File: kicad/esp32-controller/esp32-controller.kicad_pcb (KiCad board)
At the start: 2 copper layers, 100.3 x 46.4 mm, 28 parts, among them J1 Barrel_Jack_Switch, J2 RJ45, J3 RJ45, J4 RJ45, J5 RJ45, J6 Conn_01x04_Pin, U1 TPS560430, U2 SN65LVDS049, U3 SN65LVDS049, U4 ESP32-S3-WROOM-1

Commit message: Complete controller PCB v1
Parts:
- added BOOT: SW_Omron_B3FS, Button_Switch_SMD:SW_SPST_Omron_B3FS-100xP, F.Cu at (147.4, 92.0)
- added R7: 10k, Resistor_SMD:R_0805_2012Metric, F.Cu at (153.4, 84.8)
- added RESET: SW_Omron_B3FS, Button_Switch_SMD:SW_SPST_Omron_B3FS-100xP, F.Cu at (136.9, 91.9)
- moved D1 48.9 mm to (100.6, 108.0)
- moved R5 48.9 mm to (104.8, 108.0)
- moved J6 7.60 mm to (154.7, 77.7), turned to 180 degrees
- moved C2 4.51 mm to (127.6, 70.4), turned to 90 degrees
- moved R6 2.65 mm to (130.0, 73.4), turned to 0 degrees
- moved C10 2.54 mm to (130.0, 75.7)
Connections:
- net +5V renamed +12V
- U4 pad 27: unconnected-(U4-IO0-Pad27) -> Net-(U4-IO0)
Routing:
- net Net-(U4-EN): track 0.00 -> 29.9 mm, vias 0 -> 2
- net Net-(U4-IO0): track 0.00 -> 14.5 mm
- net GND: track 26.0 -> 40.4 mm, vias 19 -> 27
- net +3V3: track 0.00 -> 12.4 mm, vias 12 -> 14
- net Net-(J6-Pin_2): track 0.00 -> 4.02 mm
- net Net-(J6-Pin_3): track 0.00 -> 3.89 mm

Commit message: Cleanup
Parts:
- removed BOOT, RESET: SW_Omron_B3FS, Button_Switch_SMD:SW_SPST_Omron_B3FS-100xP
- added BOOT1: SW_Omron_B3FS, Button_Switch_SMD:SW_SPST_Omron_B3FS-100xP, F.Cu at (147.3, 91.9)
- added RESET1: SW_Omron_B3FS, Button_Switch_SMD:SW_SPST_Omron_B3FS-100xP, F.Cu at (136.9, 91.9)
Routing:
- net GND: track 40.4 -> 56.8 mm
- net +12V: track 0.00 -> 9.40 mm
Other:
- board text added: "OUT_0"
- board text added: "OUT_1"
- board text removed: "SN65LVDS049"

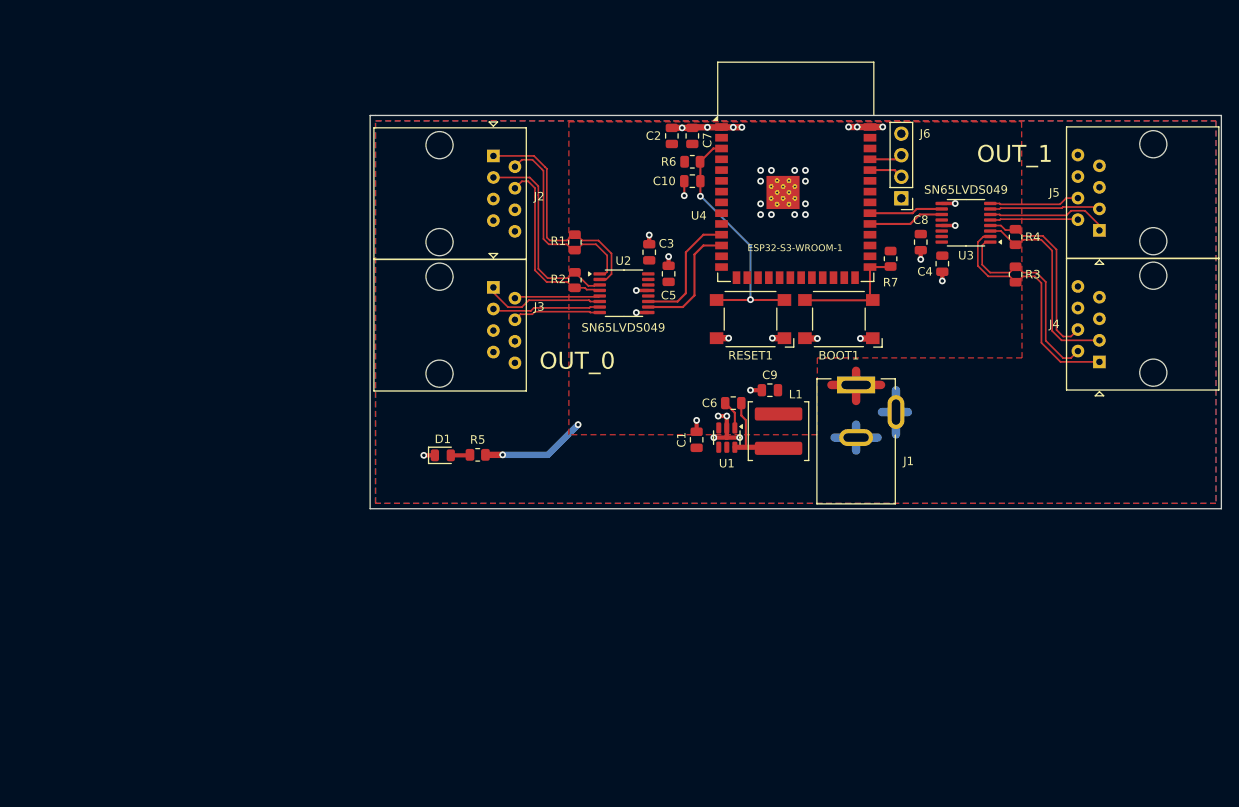
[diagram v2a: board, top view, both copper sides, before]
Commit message: Migrate to 3 chain setup
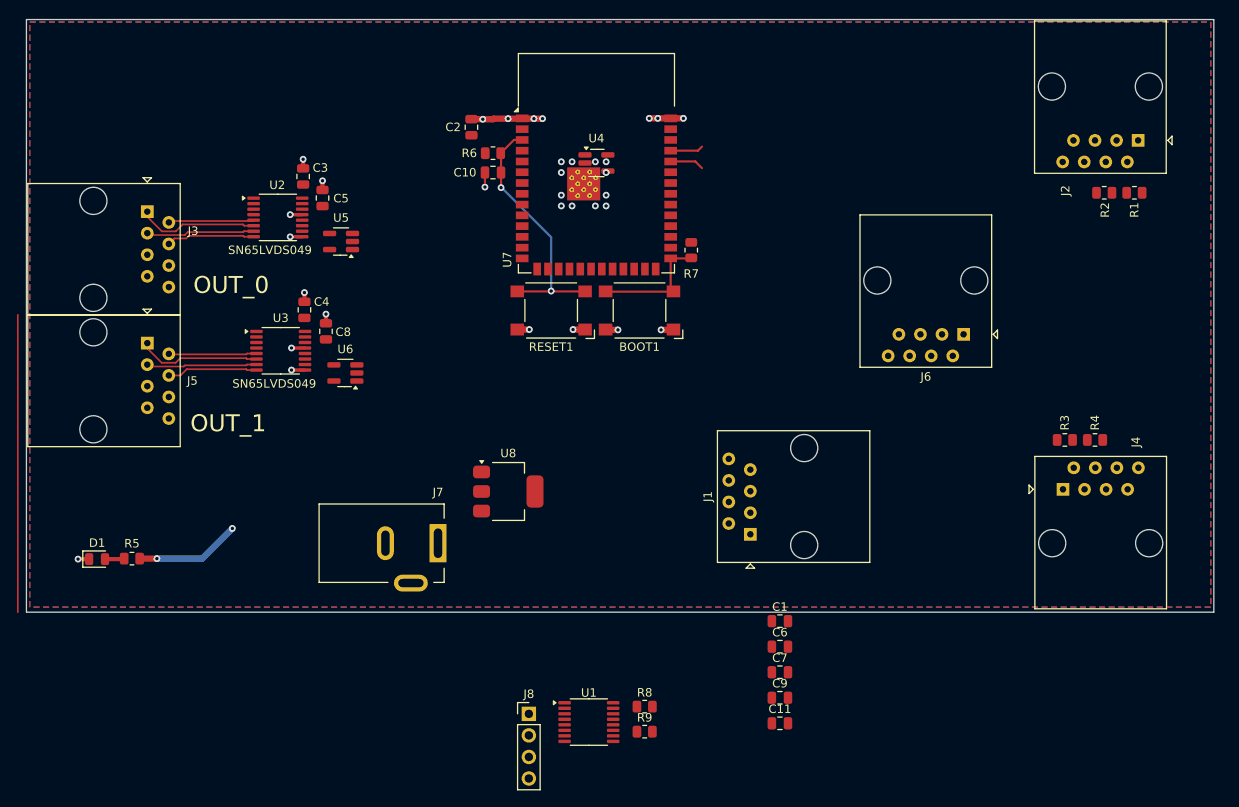
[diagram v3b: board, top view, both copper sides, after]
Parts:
- removed L1: L_Ferrite, Inductor_SMD:L_Bourns_SRP6060FA
- added C11: 100nF, Capacitor_SMD:C_0805_2012Metric, F.Cu at (140.4, 139.6)
- added J7: Barrel_Jack_Switch, Connector_BarrelJack:BarrelJack_Kycon_KLDX-0202-xC_Horizontal, F.Cu at (100.1, 118.4)
- added J8: Conn_01x04_Pin, Connector_PinHeader_2.54mm:PinHeader_1x04_P2.54mm_Vertical, F.Cu at (110.8, 138.5)
- added R8: 10k, Resistor_SMD:R_0805_2012Metric, F.Cu at (124.4, 137.6)
- added R9: 330, Resistor_SMD:R_0805_2012Metric, F.Cu at (124.4, 140.6)
- added U5: 74AHC1G08, Package_TO_SOT_SMD:SOT-23-5_HandSoldering, F.Cu at (88.6, 82.8)
- added U6: 74AHC1G08, Package_TO_SOT_SMD:SOT-23-5_HandSoldering, F.Cu at (89.2, 98.3)
- added U7: ESP32-S3-WROOM-1, RF_Module:ESP32-S3-WROOM-1, F.Cu at (118.7, 73.5)
- added U8: AZ1117-3.3, Package_TO_SOT_SMD:SOT-223-3_TabPin2, F.Cu at (108.4, 112.3)
- C1: value 2.2uF -> 100nF
- C10: value 1uF -> 100nF
- C6: value 100nF -> 4nF
- C7: value 22uF -> 1uF
- C8: value 100nF -> 10uF
- C9: value 100nF -> 22uF
- J1: value Barrel_Jack_Switch -> RJ45; footprint Connector_BarrelJack:BarrelJack_Kycon_KLDX-0202-xC_Horizontal -> Connector_RJ:RJ45_Amphenol_54602-x08_Horizontal
- J6: value Conn_01x04_Pin -> RJ45; footprint Connector_PinHeader_2.54mm:PinHeader_1x04_P2.54mm_Vertical -> Connector_RJ:RJ45_Amphenol_54602-x08_Horizontal
- R5: value 330 -> 100
- R6: value 10k -> 100
- U1: value TPS560430 -> SN65LVDS049; footprint Package_TO_SOT_SMD:SOT-23-6 -> Package_SO:TSSOP-16_4.4x5mm_P0.65mm
- U4: value ESP32-S3-WROOM-1 -> 74AHC1G08; footprint RF_Module:ESP32-S3-WROOM-1 -> Package_TO_SOT_SMD:SOT-23-5_HandSoldering
- moved J5 113.0 mm to (65.8, 94.8), turned to -90 degrees
- moved U3 82.2 mm to (81.5, 95.7), turned to 0 degrees
- moved J2 76.0 mm to (182.6, 70.9), turned to 180 degrees
- moved C4 75.4 mm to (84.3, 90.9), turned to 90 degrees
- moved C8 70.9 mm to (86.9, 93.4), turned to 90 degrees
- moved R1 66.2 mm to (182.2, 77.1), turned to 180 degrees
- moved C7 64.0 mm to (140.4, 133.6), turned to 0 degrees
- moved R2 63.2 mm to (178.6, 77.1), turned to 0 degrees
- moved D1 42.5 mm to (59.9, 120.2)
- moved R5 42.5 mm to (64.0, 120.2)
- moved C5 41.8 mm to (86.5, 77.7)
- moved U2 41.8 mm to (81.2, 80.0)
- moved C3 41.8 mm to (84.2, 75.1)
- moved J3 41.8 mm to (65.8, 79.3)
- moved U1 37.3 mm to (117.9, 139.4), turned to 0 degrees
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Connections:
- BOOT1 pad 2: Net-(U4-IO0) -> Net-(U7-IO0)
- C1 pad 1: +12V -> +3V3
- C10 pad 1: Net-(U4-EN) -> +3V3
- C6 pad 1: Net-(U1-CB) -> +3V3
- C6 pad 2: Net-(U1-SW) -> GND
- C7 pad 1: +3V3 -> Net-(U7-EN)
- C8 pad 1: +3V3 -> +12V
- J1 pad 1: +12V -> /Din_P
- J1 pad 2: GND -> /Din_N
- J1 pad 3: GND -> /Cin_N
- J2 pad 1: /Din_P -> /Dout_P
- J2 pad 2: /Din_N -> /Dout_N
- J2 pad 3: /Cin_N -> /Cout_N
- J2 pad 4: /Cin_P -> /Cout_P
- J3 pad 1: /Dout_P -> /Din_P2
- J3 pad 2: /Dout_N -> /Din_N2
- J3 pad 3: /Cout_N -> /Cin_N2
- J3 pad 4: /Cout_P -> /Cin_P2
- J4 pad 1: /Din_P2 -> /Dout_P2
- J4 pad 2: /Din_N2 -> /Dout_N2
- J4 pad 3: /Cin_N2 -> /Cout_N2
- J4 pad 4: /Cin_P2 -> /Cout_P2
- J5 pad 1: /Dout_P2 -> /Din_P2
- J5 pad 2: /Dout_N2 -> /Din_N2
- J5 pad 3: /Cout_N2 -> /Cin_N2
- J5 pad 4: /Cout_P2 -> /Cin_P2
- J6 pad 1: GND -> /Dout_P2
- J6 pad 2: Net-(J6-Pin_2) -> /Dout_N2
- J6 pad 3: Net-(J6-Pin_3) -> /Cout_N2
- J6 pad 4: +3V3 -> /Cout_P2
- R5 pad 1: +3V3 -> /Din_P2
- R5 pad 2: Net-(D1-A) -> /Din_N2
- R6 pad 1: +3V3 -> /Cin_P2
- R6 pad 2: Net-(U4-EN) -> /Cin_N2
- R7 pad 2: Net-(U4-IO0) -> Net-(U7-EN)
- RESET1 pad 2: Net-(U4-EN) -> Net-(U7-EN)
- U1 pad 1: Net-(U1-CB) -> unconnected-(U1-RIN1--Pad1)
- U1 pad 2: GND -> unconnected-(U1-RIN1+-Pad2)
- U1 pad 3: +3V3 -> unconnected-(U1-RIN2--Pad3)
- U1 pad 4: +12V -> unconnected-(U1-RIN2+-Pad4)
- U1 pad 5: +12V -> /Dout_N
- U1 pad 6: Net-(U1-SW) -> /Dout_P
- U2 pad 1: /Din_N -> unconnected-(U2-RIN1--Pad1)
- U2 pad 11: Net-(U2-DIN2) -> /MOSI
- U2 pad 2: /Din_P -> unconnected-(U2-RIN1+-Pad2)
- U2 pad 3: /Cin_N -> unconnected-(U2-RIN2--Pad3)
- U2 pad 4: /Cin_P -> unconnected-(U2-RIN2+-Pad4)
- U2 pad 5: /Dout_N -> /Dout_N2
- U2 pad 6: /Dout_P -> /Dout_P2
- U2 pad 7: /Cout_N -> /Cout_N2
- U2 pad 8: /Cout_P -> /Cout_P2
- U3 pad 1: /Din_N2 -> unconnected-(U3-RIN1--Pad1)
- U3 pad 11: Net-(U3-DIN2) -> /MOSI
- U3 pad 2: /Din_P2 -> unconnected-(U3-RIN1+-Pad2)
- U3 pad 3: /Cin_N2 -> unconnected-(U3-RIN2--Pad3)
- U3 pad 4: /Cin_P2 -> unconnected-(U3-RIN2+-Pad4)
- U4 pad 1: GND -> /SCK
- U4 pad 2: +3V3 -> unconnected-(U4-Pad2)
- U4 pad 3: Net-(U4-EN) -> +3V3
- U4 pad 4: unconnected-(U4-IO4-Pad4) -> Net-(U1-DIN1)
- U4 pad 5: unconnected-(U4-IO5-Pad5) -> GND
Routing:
- net (no net): track 0.00 -> 44.5 mm
- net Net-(U4-EN): track 29.9 -> 0.00 mm, vias 2 -> 0
- net /Din_P: track 28.1 -> 0.00 mm
- net GND: track 56.8 -> 31.1 mm, vias 27 -> 21
- net /Cin_N: track 24.6 -> 0.00 mm
- net /Cin_N2: track 24.3 -> 0.00 mm
- net /Din_N2: track 24.2 -> 0.00 mm
- net /Din_N: track 24.1 -> 0.00 mm
- net /Cin_P: track 21.8 -> 0.00 mm
- net /Cin_P2: track 21.6 -> 0.00 mm
- net /Din_P2: track 28.3 -> 12.4 mm, vias 0 -> 1
- net Net-(U2-DIN2): track 14.7 -> 0.00 mm
- net Net-(U4-IO0): track 14.5 -> 0.00 mm
- net Net-(U2-DIN1): track 14.5 -> 0.00 mm
- net +3V3: track 12.4 -> 0.00 mm, vias 14 -> 15
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- removed copper zone on F.Cu, net +3V3
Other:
- board size 100.3 x 46.4 mm -> 140 x 69.8 mm

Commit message: Complete controller pcb
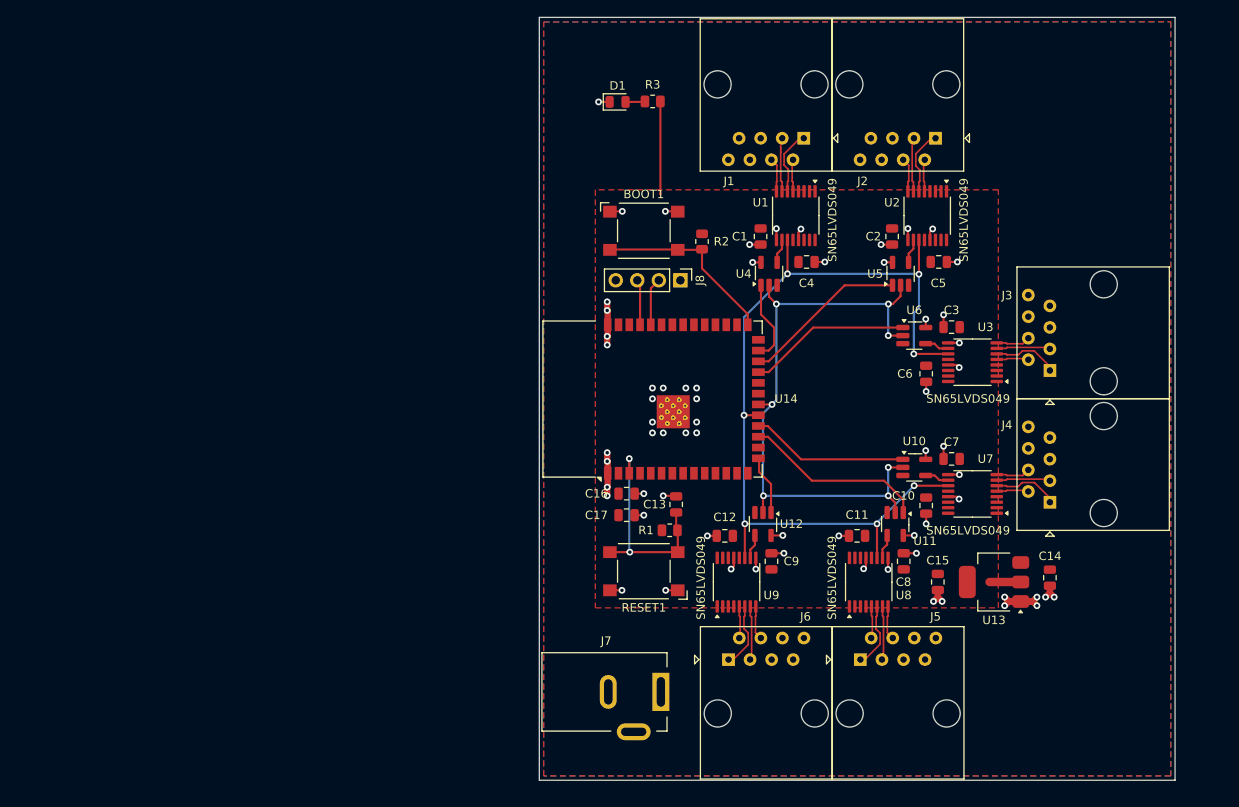
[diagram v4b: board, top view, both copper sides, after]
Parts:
- removed R4, R5, R6: 100, Resistor_SMD:R_0805_2012Metric
- removed R7, R8: 10k, Resistor_SMD:R_0805_2012Metric
- removed R9: 330, Resistor_SMD:R_0805_2012Metric
- added C12: 4nF, Capacitor_SMD:C_0805_2012Metric, F.Cu at (133.9, 117.5)
- added C13: 1uF, Capacitor_SMD:C_0805_2012Metric, F.Cu at (128.1, 113.8)
- added C14: 10uF, Capacitor_SMD:C_0805_2012Metric, F.Cu at (172.2, 122.4)
- added C15: 22uF, Capacitor_SMD:C_0805_2012Metric, F.Cu at (159.0, 122.9)
- added C16: 100nF, Capacitor_SMD:C_0805_2012Metric, F.Cu at (122.3, 112.5)
- added C17: 100nF, Capacitor_SMD:C_0805_2012Metric, F.Cu at (122.3, 115.1)
- added U10: 74AHC1G08, Package_TO_SOT_SMD:SOT-23-5_HandSoldering, F.Cu at (156.2, 109.4)
- added U11: 74AHC1G08, Package_TO_SOT_SMD:SOT-23-5_HandSoldering, F.Cu at (154.0, 116.1)
- added U12: 74AHC1G08, Package_TO_SOT_SMD:SOT-23-5_HandSoldering, F.Cu at (138.4, 116.1)
- added U13: AZ1117-3.3, Package_TO_SOT_SMD:SOT-223-3_TabPin2, F.Cu at (165.6, 122.9)
- added U14: ESP32-S3-WROOM-1, RF_Module:ESP32-S3-WROOM-1, F.Cu at (125.3, 101.4)
- added U9: SN65LVDS049, Package_SO:TSSOP-16_4.4x5mm_P0.65mm, F.Cu at (135.3, 123.0)
- C10, C11: value 100nF -> 4nF
- C7: value 1uF -> 100nF
- C8: value 10uF -> 100nF
- C9: value 22uF -> 100nF
- R1, R2: value 100 -> 10k
- R3: value 100 -> 330
- U7: value ESP32-S3-WROOM-1 -> SN65LVDS049; footprint RF_Module:ESP32-S3-WROOM-1 -> Package_SO:TSSOP-16_4.4x5mm_P0.65mm
- U8: value AZ1117-3.3 -> SN65LVDS049; footprint Package_TO_SOT_SMD:SOT-223-3_TabPin2 -> Package_SO:TSSOP-16_4.4x5mm_P0.65mm
- moved J3 108.0 mm to (172.2, 98.0), turned to 90 degrees
- moved J5 92.0 mm to (149.9, 132.1), turned to 0 degrees
- moved D1 81.7 mm to (121.2, 66.4)
- moved U3 81.5 mm to (163.1, 97.0), turned to 180 degrees
- moved C3 78.5 mm to (160.6, 92.9), turned to 180 degrees
- moved U2 76.5 mm to (157.7, 79.8), turned to -90 degrees
- moved C8 73.3 mm to (155.0, 120.5)
- moved C5 73.0 mm to (159.1, 85.2), turned to 0 degrees
- moved R1 67.7 mm to (127.4, 116.8), turned to 0 degrees
- moved U6 67.2 mm to (156.2, 93.9), turned to 0 degrees
- moved U5 66.1 mm to (154.6, 86.6), turned to 90 degrees
- moved U1 64.5 mm to (142.2, 79.8), turned to -90 degrees
- moved C10 64.4 mm to (157.6, 113.9), turned to -90 degrees
- moved R3 62.9 mm to (125.4, 66.3), turned to 180 degrees
- moved C4 59.5 mm to (143.5, 85.2), turned to 0 degrees
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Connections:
- BOOT1 pad 2: Net-(U7-IO0) -> Net-(U14-IO0)
- C7 pad 1: Net-(U7-EN) -> +3V3
- C8 pad 1: +12V -> +3V3
- J1 pad 1: /Din_P -> /Dout_P
- J1 pad 2: /Din_N -> /Dout_N
- J1 pad 3: /Cin_N -> /Cout_N
- J1 pad 4: /Cin_P -> /Cout_P
- J2 pad 1: /Dout_P -> /Dout_P2
- J2 pad 2: /Dout_N -> /Dout_N2
- J2 pad 3: /Cout_N -> /Cout_N2
- J2 pad 4: /Cout_P -> /Cout_P2
- J3 pad 1: /Din_P2 -> /Dout_P3
- J3 pad 2: /Din_N2 -> /Dout_N3
- J3 pad 3: /Cin_N2 -> /Cout_N3
- J3 pad 4: /Cin_P2 -> /Cout_P3
- J4 pad 1: /Dout_P2 -> /Dout_P4
- J4 pad 2: /Dout_N2 -> /Dout_N4
- J4 pad 3: /Cout_N2 -> /Cout_N4
- J4 pad 4: /Cout_P2 -> /Cout_P4
- J5 pad 1: /Din_P2 -> /Dout_P5
- J5 pad 2: /Din_N2 -> /Dout_N5
- J5 pad 3: /Cin_N2 -> /Cout_N5
- J5 pad 4: /Cin_P2 -> /Cout_P5
- J6 pad 1: /Dout_P2 -> /Dout_P6
- J6 pad 2: /Dout_N2 -> /Dout_N6
- J6 pad 3: /Cout_N2 -> /Cout_N6
- J6 pad 4: /Cout_P2 -> /Cout_P6
- R1 pad 1: /Din_P -> +3V3
- R1 pad 2: /Din_N -> Net-(U14-EN)
- R2 pad 1: /Cin_P -> +3V3
- R2 pad 2: /Cin_N -> Net-(U14-IO0)
- R3 pad 1: /Din_P2 -> +3V3
- R3 pad 2: /Din_N2 -> Net-(D1-A)
- RESET1 pad 2: Net-(U7-EN) -> Net-(U14-EN)
- U3 pad 5: /Dout_N2 -> /Dout_N3
- U3 pad 6: /Dout_P2 -> /Dout_P3
- U3 pad 7: /Cout_N2 -> /Cout_N3
- U3 pad 8: /Cout_P2 -> /Cout_P3
- U4 pad 1: /SCK -> /CS0
- U4 pad 2: unconnected-(U4-Pad2) -> /SCK
- U5 pad 1: /SCK -> /CS1
- U5 pad 2: unconnected-(U5-Pad2) -> /SCK
- U6 pad 1: /SCK -> /CS2
- U6 pad 2: unconnected-(U6-Pad2) -> /SCK
- U7 pad 1: GND -> unconnected-(U7-RIN1--Pad1)
- U7 pad 10: unconnected-(U7-IO17-Pad10) -> Net-(U7-DIN1)
- U7 pad 11: unconnected-(U7-IO18-Pad11) -> /MOSI
- U7 pad 12: unconnected-(U7-IO8-Pad12) -> +3V3
- U7 pad 13: unconnected-(U7-USB_D--Pad13) -> GND
- U7 pad 16: unconnected-(U7-IO46-Pad16) -> +3V3
- U7 pad 2: +3V3 -> unconnected-(U7-RIN1+-Pad2)
- U7 pad 3: Net-(U7-EN) -> unconnected-(U7-RIN2--Pad3)
- U7 pad 5: unconnected-(U7-IO5-Pad5) -> /Dout_N4
- U7 pad 6: unconnected-(U7-IO6-Pad6) -> /Dout_P4
- U7 pad 7: unconnected-(U7-IO7-Pad7) -> /Cout_N4
- U7 pad 8: unconnected-(U7-IO15-Pad8) -> /Cout_P4
- U7 pad 9: unconnected-(U7-IO16-Pad9) -> GND
- U8 pad 1: GND -> unconnected-(U8-RIN1--Pad1)
- U8 pad 2: +3V3 -> unconnected-(U8-RIN1+-Pad2)
- U8 pad 3: +12V -> unconnected-(U8-RIN2--Pad3)
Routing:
- net /MOSI: track 0.00 -> 104.6 mm, vias 0 -> 7
- net /SCK: track 0.00 -> 73.3 mm, vias 0 -> 7
- net (no net): track 44.5 -> 0.00 mm
- net GND: track 31.1 -> 72.9 mm, vias 21 -> 54
- net Net-(U14-EN): track 0.00 -> 25.7 mm, vias 0 -> 2
- net Net-(U14-IO0): track 0.00 -> 22.6 mm
- net /CS4: track 0.00 -> 21.6 mm
- net /CS1: track 0.00 -> 19.5 mm
- net /CS2: track 0.00 -> 19.2 mm
- net /CS3: track 0.00 -> 18.7 mm
- net +3V3: track 0.00 -> 14.6 mm, vias 15 -> 12
- net /Din_P2: track 12.4 -> 0.00 mm, vias 1 -> 0
- net /CS0: track 0.00 -> 9.81 mm
- net /Dout_P6: track 0.00 -> 7.80 mm
- net /Dout_P4: track 0.00 -> 7.75 mm
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- added copper zone on F.Cu, net +3V3
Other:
- board size 140 x 69.8 mm -> 74.9 x 89.9 mm
- board text removed: "OUT_0"
- board text removed: "OUT_1"

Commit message: Refactor controller pcb
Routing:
- net +3V3: vias 12 -> 0

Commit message: Fix pcb + software
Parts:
- added TP1: TestPoint, TestPoint:TestPoint_Pad_D2.0mm, F.Cu at (131.3, 89.9)
- added TP2: TestPoint, TestPoint:TestPoint_Pad_D2.0mm, F.Cu at (131.3, 86.7)
- moved J8 0.63 mm to (128.0, 87.4)
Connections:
- U10 pad 3: +3V3 -> GND
- U10 pad 5: GND -> +3V3
- U11 pad 3: +3V3 -> GND
- U11 pad 5: GND -> +3V3
- U12 pad 3: +3V3 -> GND
- U12 pad 5: GND -> +3V3
- U14 pad 31: unconnected-(U14-IO38-Pad31) -> Net-(U14-IO38)
- U14 pad 32: unconnected-(U14-IO39-Pad32) -> Net-(U14-IO39)
- U4 pad 3: +3V3 -> GND
- U4 pad 5: GND -> +3V3
- U5 pad 3: +3V3 -> GND
- U5 pad 5: GND -> +3V3
- U6 pad 3: +3V3 -> GND
- U6 pad 5: GND -> +3V3
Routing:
- net Net-(U14-IO39): track 0.00 -> 6.80 mm
- net Net-(U14-IO38): track 0.00 -> 2.79 mm
- net GND: track 72.9 -> 74.7 mm
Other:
- board text added: "+V"
- board text added: "GND"
- board text added: "RX"
- board text added: "TX"
